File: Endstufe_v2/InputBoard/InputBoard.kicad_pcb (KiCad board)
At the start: 4 copper layers, 85 x 50 mm, 65 parts, among them J1 ST-0322D00-071-1A2H, J11 DNP, J2 ST-0322D00-071-1A2H, J3 ST-0322D00-071-1A2H, J4 ST-0322D00-071-1A2H, J5 B4B-XH-2_(LF)(SN), J6 B4B-XH-2_(LF)(SN), J7 B4B-XH-2_(LF)(SN), J8 Conn_01x02_Pin, J9 B4B-XH-2_(LF)(SN), U1 PCM1865DBTR, U2 PCM9211PTR, U4 ZPLR135_T8, U5 ZPLR135_T8, U6 ZPLR135_T8, U7 ZPLR135_T8, Y1 24.576Mhz, Y2 24.576Mhz

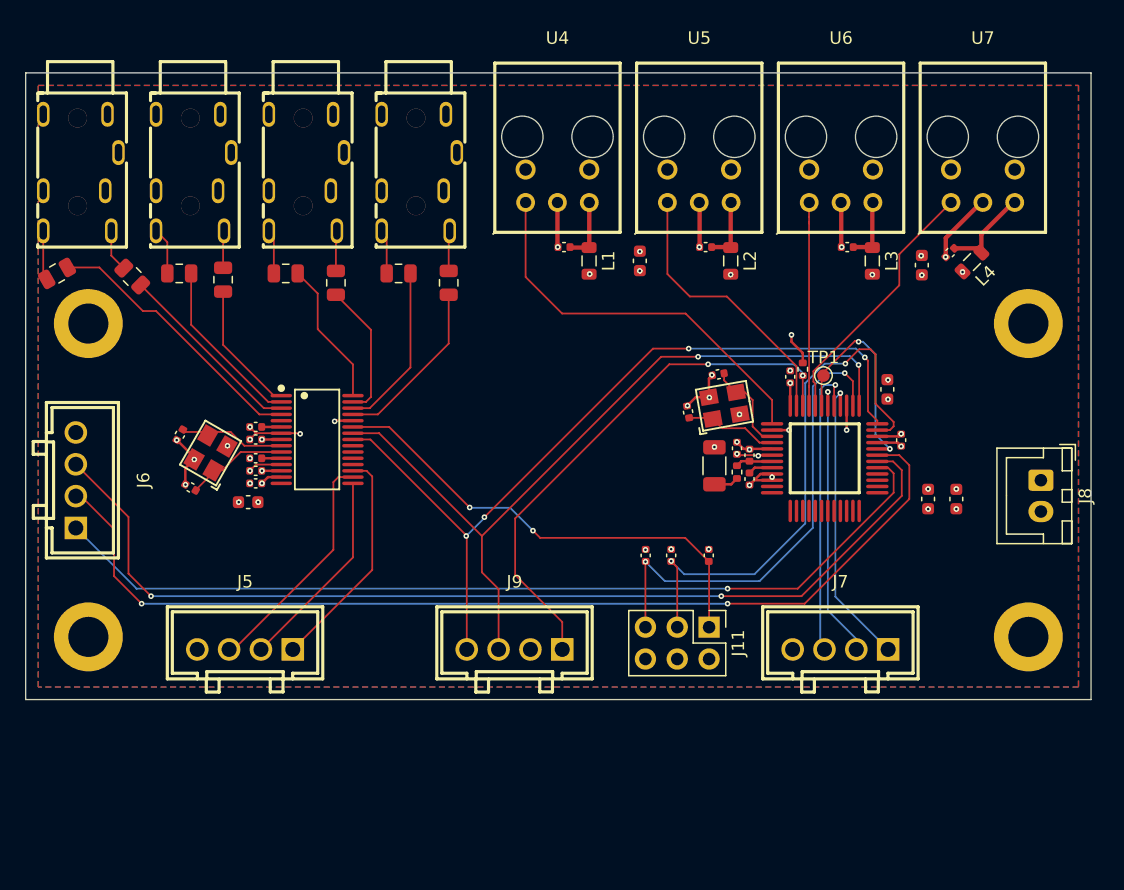
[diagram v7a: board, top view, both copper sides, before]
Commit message: Optimise placing of silkscreen
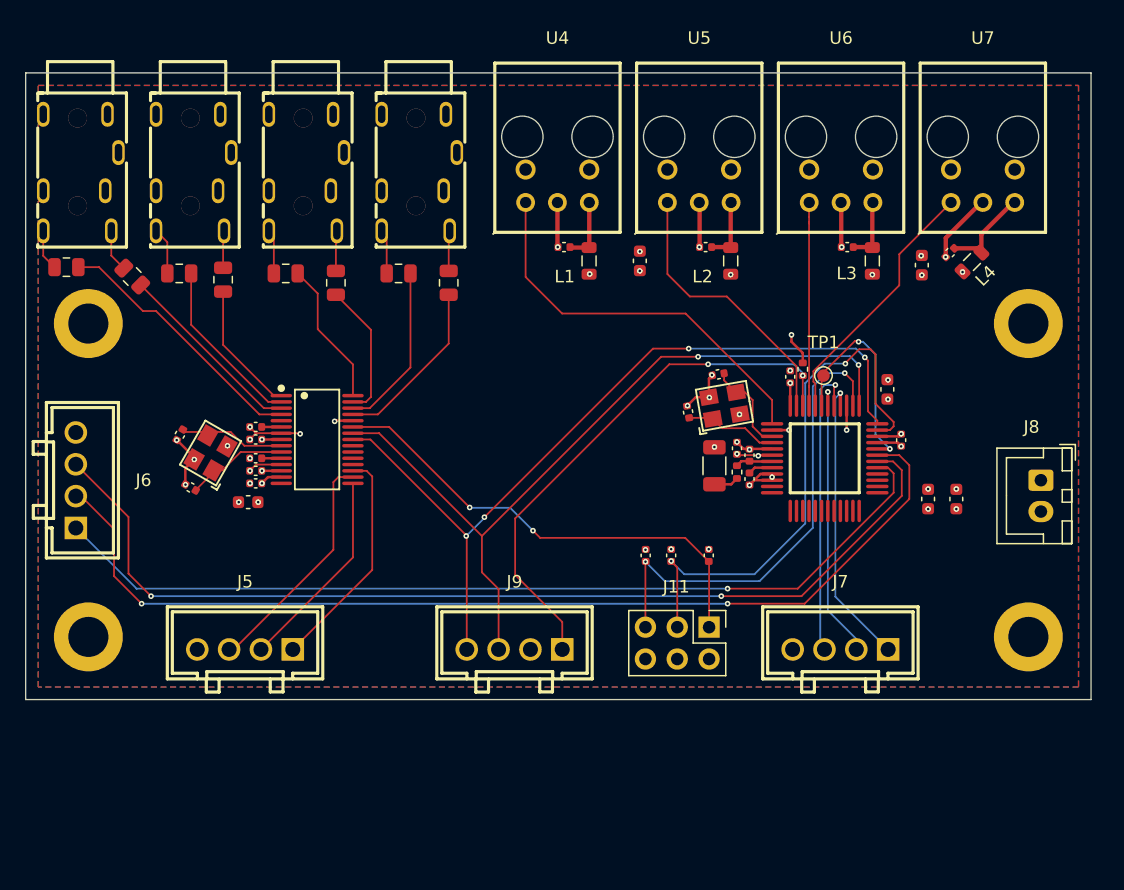
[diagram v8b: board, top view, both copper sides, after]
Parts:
- moved C2 0.90 mm to (73.2, 85.5), turned to 0 degrees
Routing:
- net /PCM1865/VINR1: track 21.9 -> 21.1 mm
- net Net-(J1-AUDIO_R): track 3.98 -> 3.27 mm
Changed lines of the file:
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@@
 	(footprint "Endstufe:C_0805_2012Metric"
 		(layer "F.Cu")
-		(at 72.5 86 30)
+		(at 73.25 85.5)
 		(descr "Capacitor SMD 0805 (2012 Metric), square (rectangular) end terminal, IPC_7351 nominal, (Body size source: IPC-SM-782 page 76, https://www.pcb-3d.com/wordpress/wp-content/uploads/ipc-sm-782a_amendment_1_and_2.pdf, https://docs.google.com/spreadsheets/d/1BsfQQcO9C6DZCsRaXUlFlo91Tg2WpOkGARC1WS5S8t0/edit?usp=sharing), generated with kicad-footprint-generator")
 		(tags "capacitor")
 		(property "Reference" "C2"
-			(at 0 -1.68 30)
+			(at 0 -1.68 0)
 			(layer "F.SilkS")
 			(hide yes)
@@
 		)
 		(property "Value" "10uF"
-			(at 0 1.68 30)
+			(at 0 1.68 0)
 			(layer "F.Fab")
 			(effects
@@
 		)
 		(property "Footprint" "Endstufe:C_0805_2012Metric"
-			(at 0 0 30)
+			(at 0 0 0)
 			(layer "F.Fab")
 			(hide yes)
@@
 		)
 		(property "Datasheet" ""
-			(at 0 0 30)
+			(at 0 0 0)
 			(layer "F.Fab")
 			(hide yes)
@@
 		)
 		(property "Description" ""
-			(at 0 0 30)
+			(at 0 0 0)
 			(layer "F.Fab")
 			(hide yes)
@@
 		)
 		(property "LCSC Part #" "C15850"
-			(at 0 0 30)
+			(at 0 0 0)
 			(layer "F.Fab")
 			(hide yes)
@@
 		)
 		(fp_text user "${REFERENCE}"
-			(at 0 0 30)
+			(at 0 0 0)
 			(layer "F.Fab")
 			(effects
@@
 		)
 		(pad "1" smd roundrect
-			(at -0.95 0 30)
+			(at -0.95 0)
 			(size 1 1.45)
 			(layers "F.Cu" "F.Paste" "F.Mask")
@@
 		)
 		(pad "2" smd roundrect
-			(at 0.95 0 30)
+			(at 0.95 0)
 			(size 1 1.45)
 			(layers "F.Cu" "F.Paste" "F.Mask")
@@
 		(tags "Through hole pin header THT 2x03 2.54mm double row")
 		(property "Reference" "J11"
-			(at 1.27 -2.33 90)
+			(at -3.225 2.625 0)
 			(layer "F.SilkS")
 			(effects
@@
 		(tags "inductor")
 		(property "Reference" "L3"
-			(at 0 -1.55 90)
+			(at 1 2.05 180)
 			(layer "F.SilkS")
 			(effects
@@
 		(tags "connector JST XH vertical")
 		(property "Reference" "J8"
-			(at 1.25 -3.55 90)
+			(at -4.25 0.75 180)
 			(layer "F.SilkS")
 			(effects
@@
 		(tags "inductor")
 		(property "Reference" "L1"
-			(at 0 -1.55 90)
+			(at 1.25 1.95 180)
 			(layer "F.SilkS")
 			(effects
@@
 		(tags "inductor")
 		(property "Reference" "L2"
-			(at 0 -1.55 90)
+			(at 1.25 2.25 180)
 			(layer "F.SilkS")
 			(effects
@@
 		(tags "CONN-TH_B4B-XH-2-LF-SN footprint C157999")
 		(property "Reference" "J6"
-			(at 0 -5.4 90)
+			(at 0 -5.4 180)
 			(layer "F.SilkS")
 			(effects
@@
 		(tags "test point SMD pad")
 		(property "Reference" "TP1"
-			(at 0 -1.448 0)
+			(at 0 -2.65 0)
 			(layer "F.SilkS")
 			(effects
@@
 	)
 	(segment
-		(start 79.35 89)
-		(end 75.875 85.525)
+		(start 88.65 97.25)
+		(end 80.4 89)
 		(width 0.1427)
 		(layer "F.Cu")
@@
 	)
 	(segment
-		(start 80.4 89)
-		(end 79.35 89)
+		(start 75.85 85.5)
+		(end 74.2 85.5)
 		(width 0.1427)
 		(layer "F.Cu")
@@
 	)
 	(segment
-		(start 90.39 97.25)
-		(end 88.65 97.25)
+		(start 79.35 89)
+		(end 75.85 85.5)
 		(width 0.1427)
 		(layer "F.Cu")
@@
 	)
 	(segment
-		(start 88.65 97.25)
-		(end 80.4 89)
+		(start 80.4 89)
+		(end 79.35 89)
 		(width 0.1427)
 		(layer "F.Cu")
@@
 	)
 	(segment
-		(start 75.875 85.525)
-		(end 73.322724 85.525)
+		(start 90.39 97.25)
+		(end 88.65 97.25)
 		(width 0.1427)
 		(layer "F.Cu")
@@
 	)
 	(segment
-		(start 71.4 86.197724)
-		(end 71.677276 86.475)
+		(start 71.4 82.605)
+		(end 71.4 84.6)
 		(width 0.1427)
 		(layer "F.Cu")
@@
 	)
 	(segment
-		(start 71.4 82.605)
-		(end 71.4 86.197724)
+		(start 71.4 84.6)
+		(end 72.3 85.5)
 		(width 0.1427)
 		(layer "F.Cu")
